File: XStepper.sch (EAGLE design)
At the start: 69 parts, among them IC1 LM7805, Q2 16 MHZ

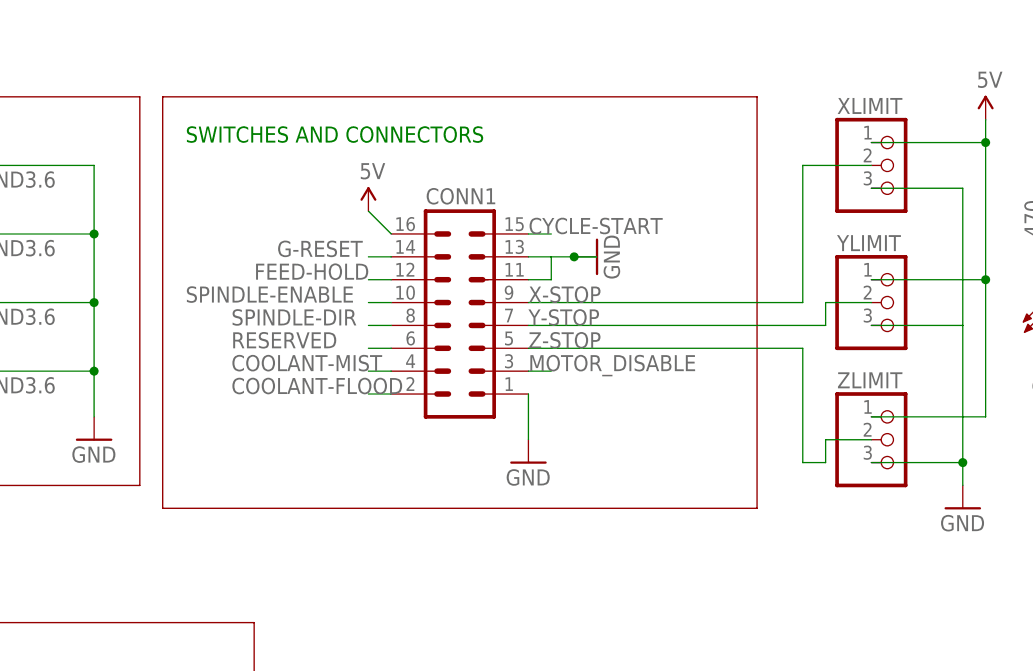
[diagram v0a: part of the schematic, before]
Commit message: add pullup resistors for Hallo Sensor switches (Cherry MP101401)
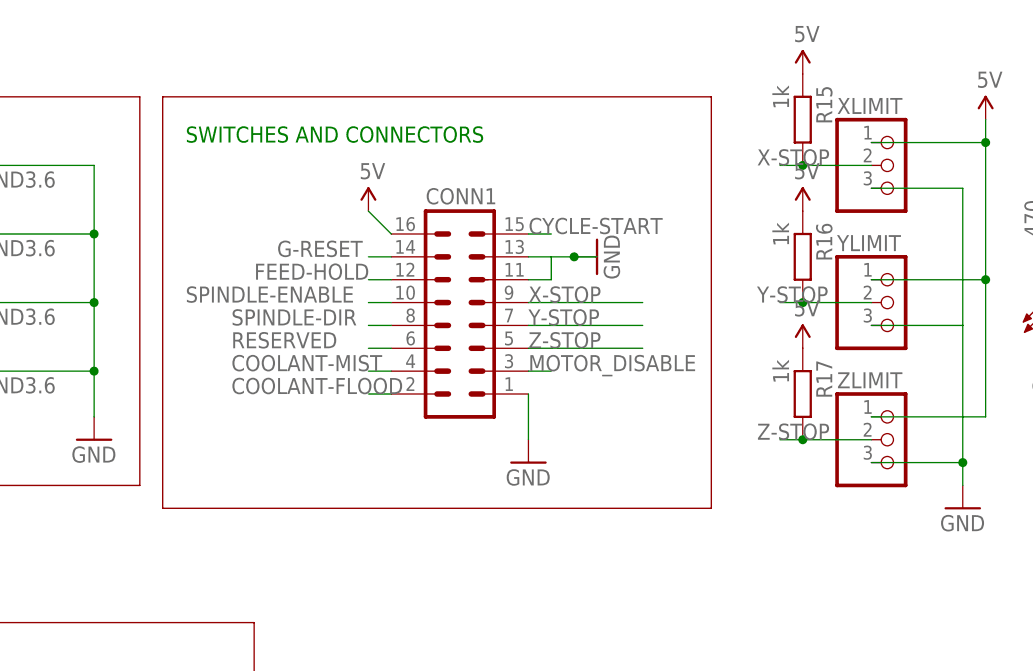
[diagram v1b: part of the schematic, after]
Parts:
- added R15, R16, R17: 1k, resistor:R-EU_0204/2V
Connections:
- net 5V: now also R15.1, R16.1, R17.1
- net X-STOP: now also R15.2
- net Y-STOP: now also R16.2
- net Z-STOP: now also R17.2

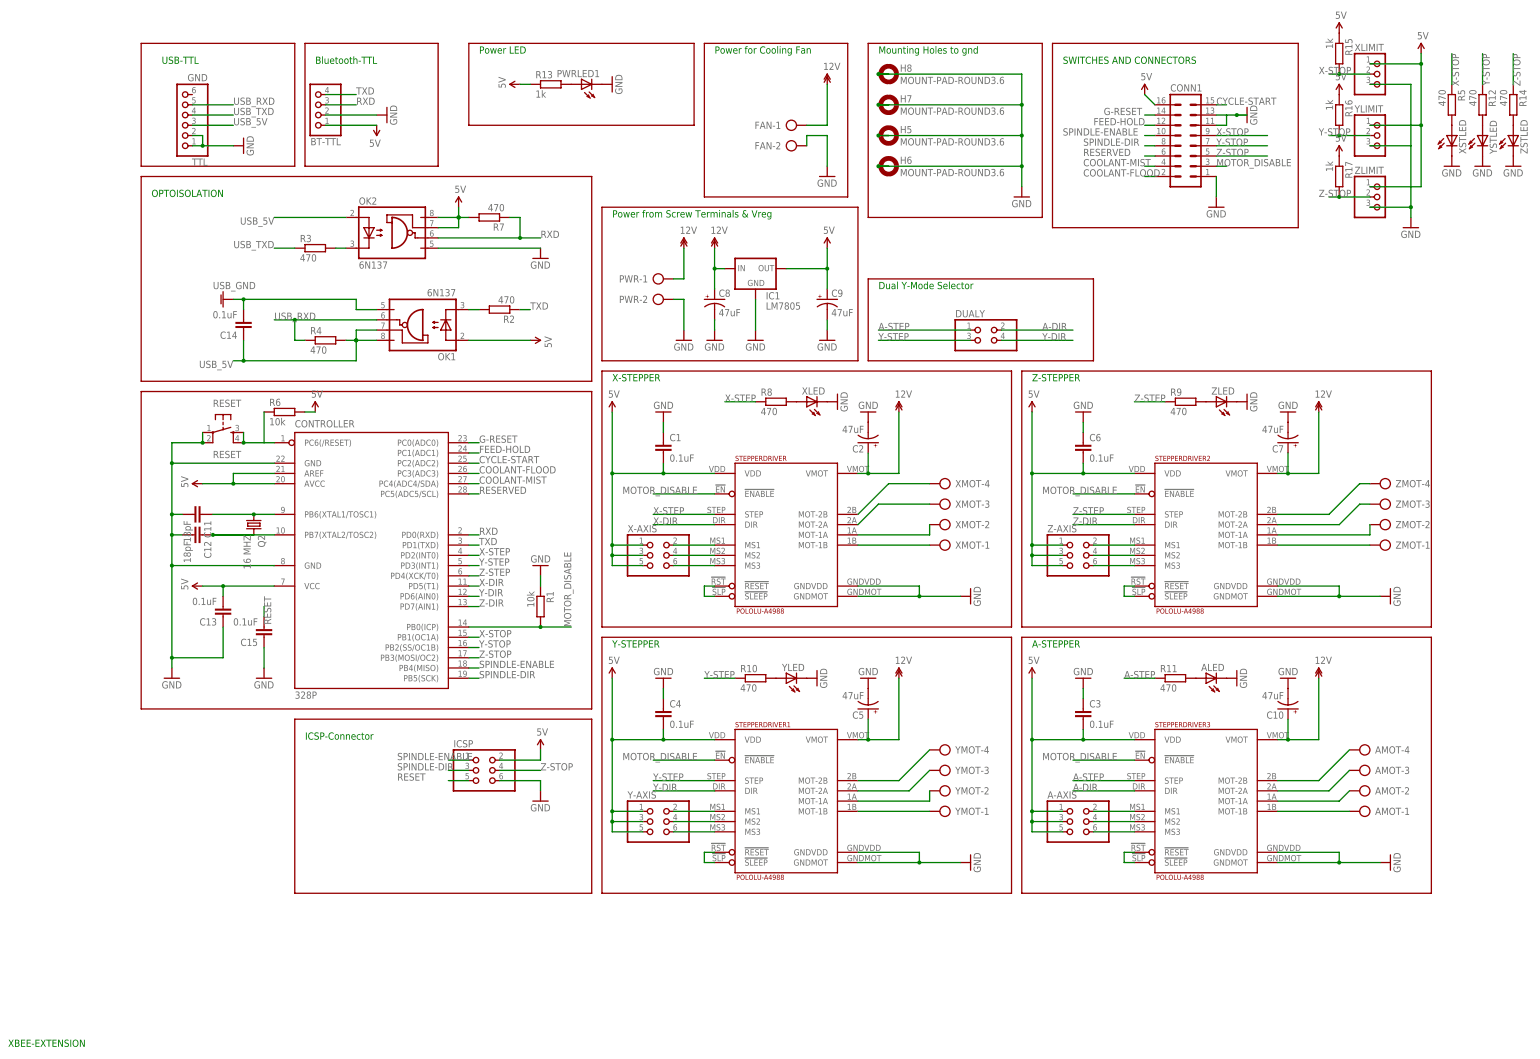
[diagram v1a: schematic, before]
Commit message: Bugfree version from 0.9 to produce in ITEAD
Version 0.91 from Matt to produce without bugs
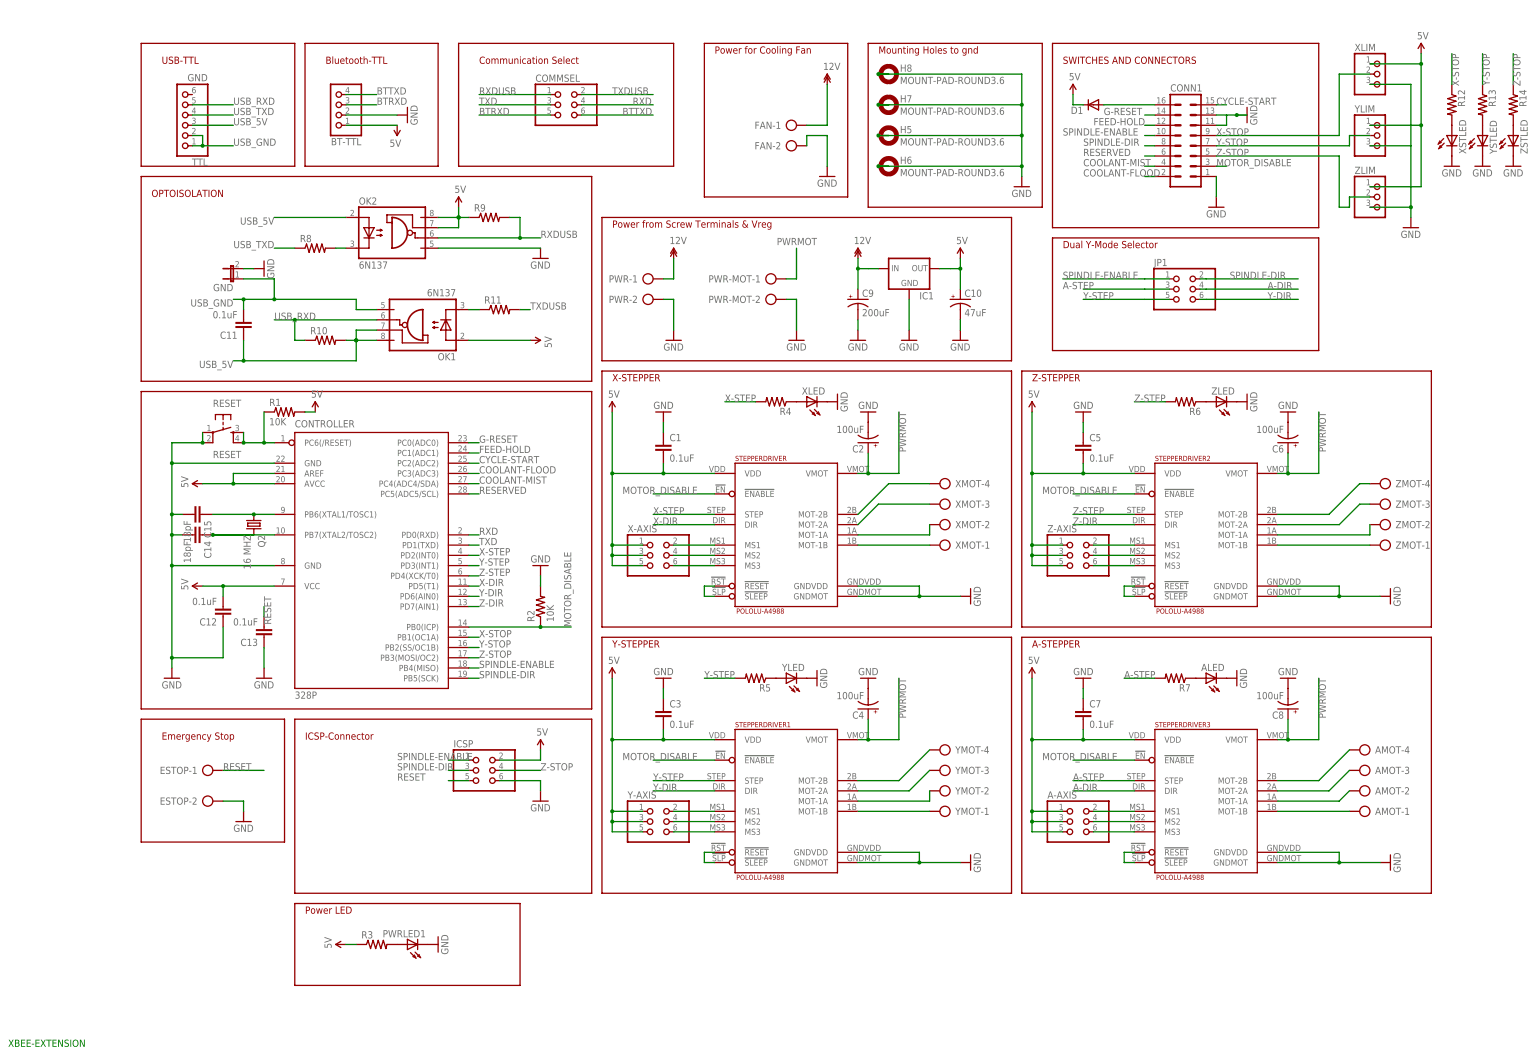
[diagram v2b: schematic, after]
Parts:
- removed DUALY: (no value), pinhead:PINHD-2X2
- removed R15, R16, R17: 1k, resistor:R-EU_0204/2V
- added COMMSEL, JP1: (no value), pinhead:PINHD-2X3
- added D1: (no value), SparkFun-DiscreteSemi:DIODEPTH
- added ESTOP, PWR-MOT: (no value), con-ptr500:AK500/2
- added GND: (no value), jumper:JP1E
- C11, C12: value 18pF -> 0.1uF
- C14, C15: value 0.1uF -> 18pF
- C2, C8: value 47uF -> 100uF
- C4, C6: value 0.1uF -> 100uF; device resistor:C-EU025-025X050 -> resistor:CPOL-USE2.5-6
- C5, C7: value 47uF -> 0.1uF; device resistor:CPOL-USE2.5-6 -> resistor:C-EU025-025X050
- C9: value 47uF -> 200uF
- IC1: value LM7805 -> (none); device SparkFun:V_REG_78XX -> SparkFun-PowerIC:V_REG_78XXSINK
- R1: value 10k -> 10K; device resistor:R-EU_0204/5 -> SparkFun-Resistors:RESISTORAXIAL-0.3
- R10, R11, R12, R14, R5, R8, R9: value 470 -> (none); device resistor:R-EU_0204/2V -> SparkFun-Resistors:RESISTORAXIAL-0.3
- R13: value 1k -> (none); device resistor:R-EU_0204/2V -> SparkFun-Resistors:RESISTORAXIAL-0.3
- R2: value 470 -> 10K; device resistor:R-EU_0204/5 -> SparkFun-Resistors:RESISTORAXIAL-0.3
- R3, R4, R7: value 470 -> (none); device resistor:R-EU_0204/5 -> SparkFun-Resistors:RESISTORAXIAL-0.3
- R6: value 10k -> (none); device resistor:R-EU_0204/5 -> SparkFun-Resistors:RESISTORAXIAL-0.3
- renumbered XLIMIT to XLIM, YLIMIT to YLIM, ZLIMIT to ZLIM
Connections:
- removed net GNDA: C14.2, OK1.GND
- new net BTRXD: BT-TTL.3, COMMSEL.5
- new net BTTXD: BT-TTL.4, COMMSEL.6
- new net N$45: CONN1.16, D1.A
- new net PWRMOT: C2.+, C4.+, C6.+, C8.+, PWR-MOT-1.KL, STEPPERDRIVER.VMOT, STEPPERDRIVER1.VMOT, STEPPERDRIVER2.VMOT, STEPPERDRIVER3.VMOT
- new net RXDUSB: COMMSEL.1, OK2.VO, R9.2
- new net TXDUSB: COMMSEL.2, R11.2
- new net USB_GND: C11.2, GND.1, OK1.GND, TTL.1, TTL.2
- net 12V: now also C9.+; no longer C10.+, C2.+, C5.+, C7.+, C8.+, STEPPERDRIVER.VMOT, STEPPERDRIVER1.VMOT, STEPPERDRIVER2.VMOT, STEPPERDRIVER3.VMOT
- net 5V: now also C10.+, C12.2, C5.2, C7.2, D1.C, R1.2, R3.1, R9.1; no longer C13.2, C4.2, C6.2, C9.+, CONN1.16, R13.1, R15.1, R16.1, R17.1, R6.2, R7.2
- net A-DIR: now also JP1.4; no longer DUALY.2
- net A-STEP: now also JP1.3, R7.2; no longer DUALY.1, R11.1
- net GND: now also C12.1, C14.2, C15.2, C4.-, C5.1, C6.-, C7.1, ESTOP-2.KL, GND.2, PWR-MOT-2.KL, R2.2; no longer C11.2, C12.2, C15.1, C4.1, C5.-, C6.1, C7.-, R1.1, TTL.1, TTL.2
- net MOTOR_DISABLE: now also R2.1; no longer R1.2
- net N$33: now also C15.1; no longer C11.1
- net N$34: now also C14.1; no longer C12.1
- net N$35: now also R8.2; no longer R3.2
- net N$36: now also R11.1; no longer R2.2
- net N$37: now also R12.2; no longer R5.2
- net N$38: now also R4.1; no longer R8.2
- net N$39: now also R5.1, YLED.A; no longer R9.2, ZLED.A
- net N$40: now also R6.1, ZLED.A; no longer R10.2, YLED.A
- net N$41: now also R7.1; no longer R11.2
- net N$42: now also R13.2; no longer R12.2
- net N$43: now also R3.2; no longer R13.2
- net RESET: now also C13.2, ESTOP-1.KL, R1.1; no longer C15.2, R6.1
- net RXD: now also COMMSEL.4; no longer BT-TTL.3, OK2.VO, R7.1
- net SPINDLE-DIR: now also JP1.2
- net SPINDLE-ENABLE: now also JP1.1
- net TXD: now also COMMSEL.3; no longer BT-TTL.4, R2.1
- net USB_5V: now also C11.1, R10.2; no longer C14.1, R4.2
- net USB_RXD: now also R10.1; no longer R4.1
- net USB_TXD: now also R8.1; no longer R3.1
- net X-STEP: now also R4.2; no longer R8.1
- net X-STOP: now also R12.1; no longer R15.2, R5.1
- net Y-DIR: now also JP1.6; no longer DUALY.4
- net Y-STEP: now also JP1.5, R5.2; no longer DUALY.3, R10.1
- net Y-STOP: now also R13.1; no longer R12.1, R16.2
- net Z-STEP: now also R6.2; no longer R9.1
- net Z-STOP: no longer R17.2
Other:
- note added: "Communication Select"
- note added: "Emergency Stop"
- moved on the sheet: BT-TTL, C10, C11, C12, C13, C14, C15, C3, C8, C9, IC1, PWR-1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

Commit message: - change header ICSP
- more space between caps at 7805
- add VCC area on top to save wires
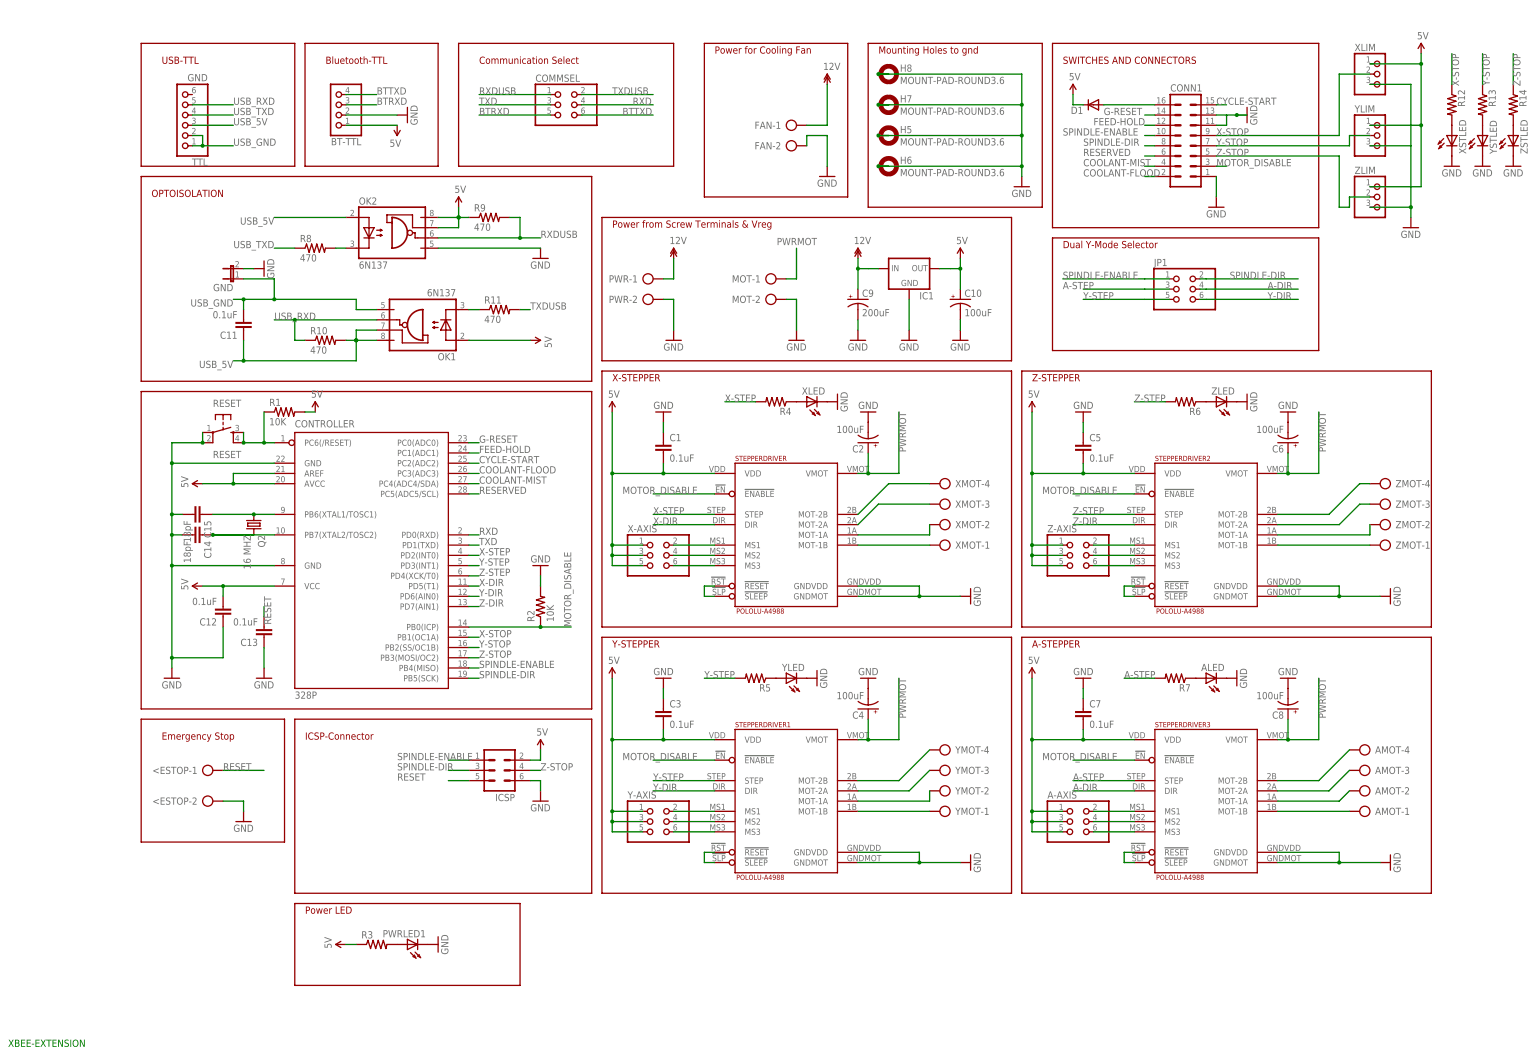
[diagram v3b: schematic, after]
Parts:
- C10: value 47uF -> 100uF
- ICSP: device pinhead:PINHD-2X3 -> con-ml:ML6
- R10, R11, R8, R9: value (none) -> 470
- renumbered ESTOP to <ESTOP, PWR-MOT to MOT
